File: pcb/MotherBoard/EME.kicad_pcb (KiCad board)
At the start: 2 copper layers, 100 x 60 mm, 48 parts, among them J1 BMP180, J10 Reset, J11 UART2, J12 SPI_CONN, J13 UART0, J14 MQ135, J15 5v, J16 GPIO's, J17 Anemómetro, J19 I2C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

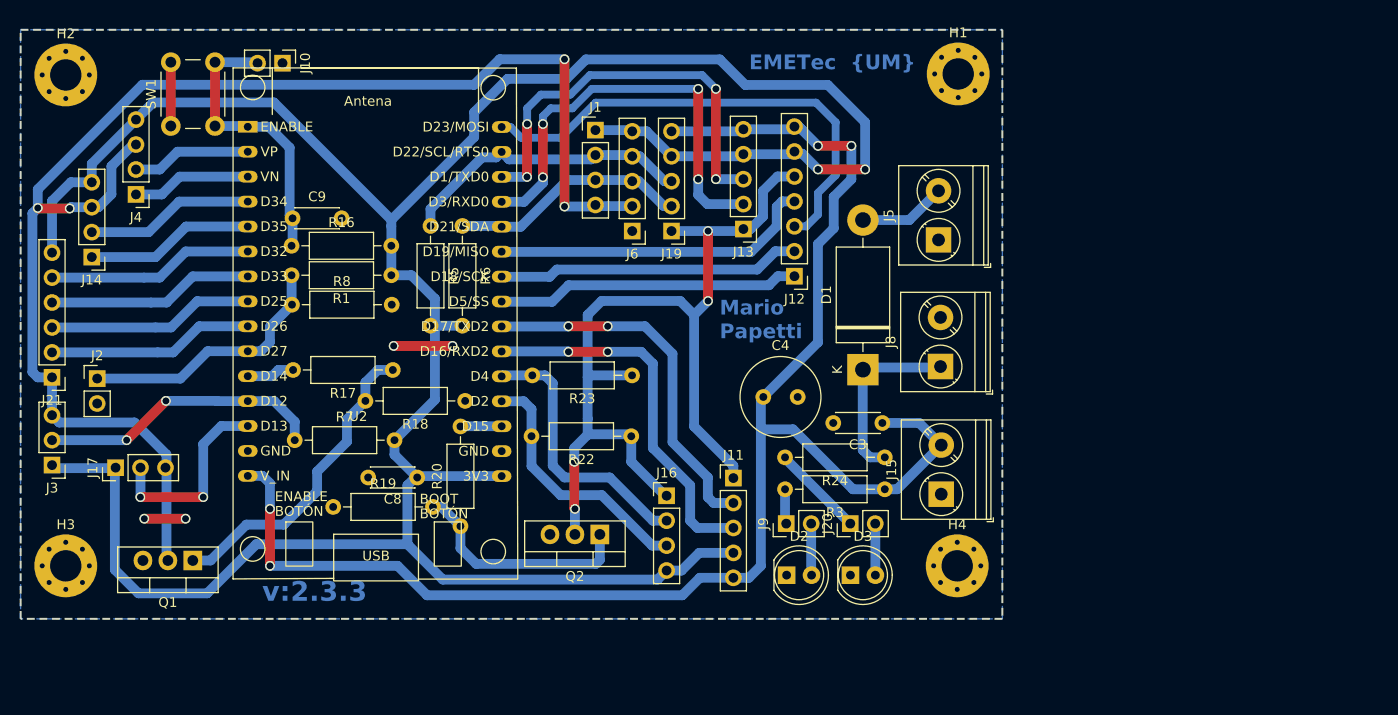
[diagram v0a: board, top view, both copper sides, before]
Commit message: se readaptaron y revisaron las PCBs, listas para imprimir
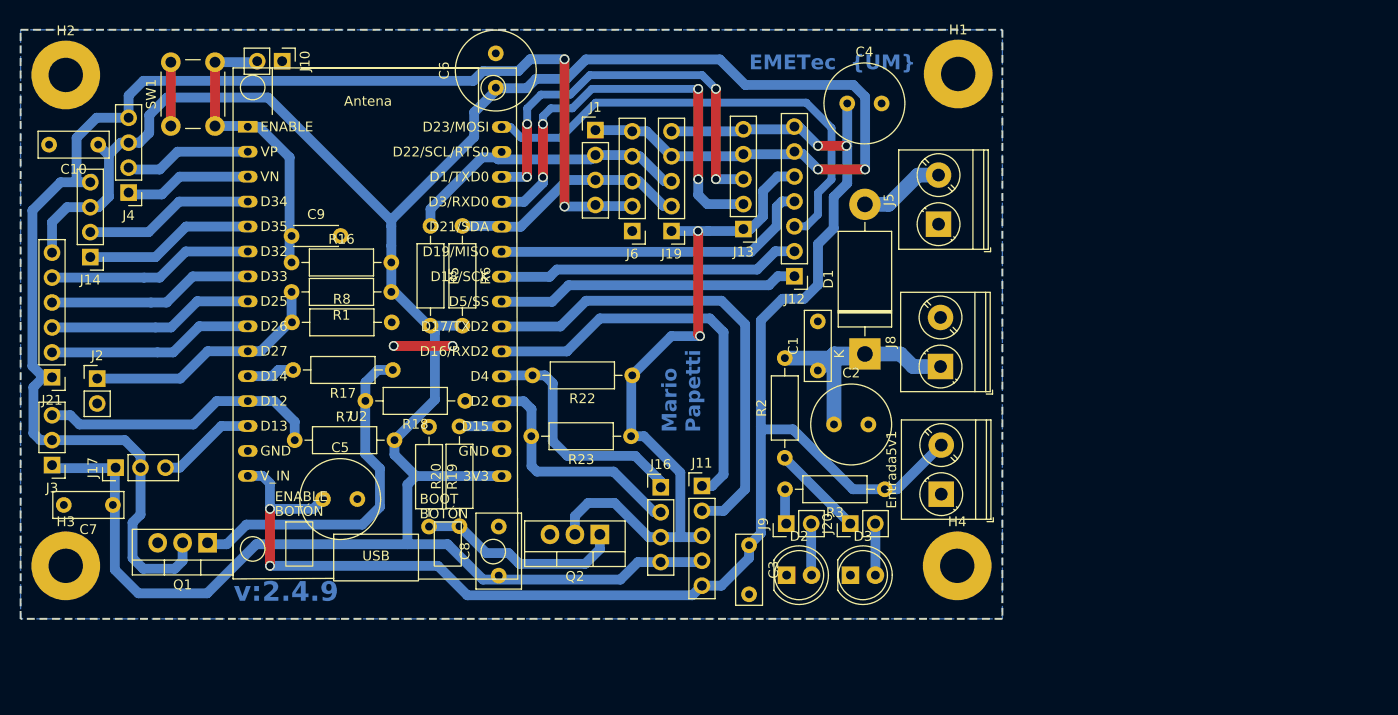
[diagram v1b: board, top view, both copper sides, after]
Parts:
- removed R24: 1k, Resistor_THT:R_Axial_DIN0207_L6.3mm_D2.5mm_P10.16mm_Horizontal
- added C1: 104, Capacitor_THT:C_Disc_D7.0mm_W2.5mm_P5.00mm, F.Cu at (112.4, 89.5)
- added C10: 104, Capacitor_THT:C_Disc_D7.0mm_W2.5mm_P5.00mm, F.Cu at (39.1, 66.5)
- added C2: 220uF, Capacitor_THT:C_Radial_D8.0mm_H11.5mm_P3.50mm, F.Cu at (114.0, 95.0)
- added C5: 22uF, Capacitor_THT:C_Radial_D8.0mm_H7.0mm_P3.50mm, F.Cu at (62.0, 102.6)
- added C6: 22uF, Capacitor_THT:C_Radial_D8.0mm_H7.0mm_P3.50mm, F.Cu at (79.6, 60.7)
- added C7: 104, Capacitor_THT:C_Disc_D7.0mm_W2.5mm_P5.00mm, F.Cu at (40.6, 103.2)
- added R2: 1k, Resistor_THT:R_Axial_DIN0207_L6.3mm_D2.5mm_P10.16mm_Horizontal, F.Cu at (109.0, 98.4)
- C3: footprint Capacitor_THT:C_Disc_D4.3mm_W1.9mm_P5.00mm -> Capacitor_THT:C_Disc_D7.0mm_W2.5mm_P5.00mm
- C8: footprint Capacitor_THT:C_Disc_D4.3mm_W1.9mm_P5.00mm -> Capacitor_THT:C_Disc_D7.5mm_W4.4mm_P5.00mm
- H1, H2, H3, H4: footprint MountingHole:MountingHole_3.2mm_M3_Pad_Via -> MountingHole:MountingHole_3.5mm_Pad
- moved C4 31.1 mm to (115.4, 62.3)
- moved C3 18.4 mm to (105.4, 107.3), turned to -90 degrees
- moved C8 13.0 mm to (79.9, 110.4), turned to 90 degrees
- moved R19 12.7 mm to (72.8, 95.2), turned to -90 degrees
- moved R23 6.20 mm to (93.4, 96.2)
- moved R22 6.20 mm to (93.5, 90.0)
- moved J11 3.30 mm to (100.6, 101.3)
- moved Q1 2.34 mm to (50.2, 107.1)
- moved C9 1.80 mm to (58.8, 75.8)
- moved R8 1.80 mm to (58.8, 84.6)
- moved R1 1.70 mm to (69.0, 81.5)
- moved R16 1.70 mm to (58.8, 78.5)
- moved D1 1.61 mm to (117.2, 87.8)
- moved J5 1.60 mm to (124.7, 74.6)
- moved J16 1.05 mm to (96.4, 101.4)
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- renumbered J15 to Entrada5v1
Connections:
- H1 pad 1: (no net) -> GNDREF
- H2 pad 1: (no net) -> GNDREF
- H3 pad 1: (no net) -> GNDREF
- H4 pad 1: (no net) -> GNDREF
- J11 pad 1: GND_G2 -> RX2
- J11 pad 3: RX2 -> GND_G2
- J14 pad 3: GND_G1 -> +3.3V
- J14 pad 4: +3.3V -> GND_G1
- J16 pad 1: GND_G2 -> GPIO4
- J16 pad 2: GPIO4 -> GPIO13
- J16 pad 3: GPIO13 -> GND_G2
- J17 pad 2: D_hall -> GND_G1
- J17 pad 3: GND_G1 -> D_hall
- J3 pad 2: DHT22 -> GND_G1
- J3 pad 3: GND_G1 -> DHT22
- J4 pad 3: GND_G1 -> +3.3V
- J4 pad 4: +3.3V -> GND_G1
- R22 pad 2: GPIO13 -> GPIO4
- R23 pad 2: GPIO4 -> GPIO13
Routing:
- net GND_G2: track 95.6 -> 71.9 mm, vias 4 -> 2
- net TX2: track 37.5 -> 49.0 mm, vias 2 -> 0
- net +BATT: track 18.6 -> 29.3 mm
- net D_hall: track 20.3 -> 10.3 mm, vias 2 -> 0
- net GNDREF: track 16.7 -> 12.5 mm, vias 4 -> 2
- net Net-(Q1-G): track 32.2 -> 36.1 mm
- net RX2: track 38.2 -> 42.0 mm, vias 2 -> 0
- net GPIO4: track 27.9 -> 24.8 mm
- net +5V: track 159.7 -> 162.4 mm
- net Net-(Q2-G): track 23.5 -> 21.1 mm
- net GPIO13: track 26.3 -> 24.4 mm
- net Div: track 26.9 -> 25.2 mm
- net GND_G1: track 144.6 -> 143.3 mm, vias 4 -> 2
- net Rest: track 29.6 -> 30.6 mm
- net MOSI: track 49.8 -> 48.9 mm
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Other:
- board text added: "v:2.4.9"
- board text removed: "v:2.3.3"

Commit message: Se agregó la modificación del MQ135 a 5v con divisor resistivo; además de cambio del DHT del pin 12; también se modificaron los pines de conexión
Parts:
- removed J16: GPIO's, Connector_PinHeader_2.54mm:PinHeader_1x04_P2.54mm_Vertical
- added C11: 22uF, Capacitor_THT:C_Radial_D8.0mm_H7.0mm_P3.50mm, F.Cu at (143.1, 66.4)
- added C12: 104, Capacitor_THT:C_Disc_D7.0mm_W2.5mm_P5.00mm, F.Cu at (106.2, 114.9)
- added J7: MQ135, Connector_PinHeader_2.54mm:PinHeader_1x03_P2.54mm_Vertical, F.Cu at (80.9, 104.8)
- added R10: 22k, Resistor_THT:R_Axial_DIN0207_L6.3mm_D2.5mm_P10.16mm_Horizontal, F.Cu at (76.8, 98.4)
- added R9: 12k, Resistor_THT:R_Axial_DIN0207_L6.3mm_D2.5mm_P10.16mm_Horizontal, F.Cu at (76.8, 101.4)
- J14: value MQ135 -> GPIO's; footprint Connector_PinHeader_2.54mm:PinHeader_1x04_P2.54mm_Vertical -> Connector_PinHeader_2.54mm:PinHeader_1x05_P2.54mm_Vertical
- R1: value 4k7 -> 1M
- R8: value 4k7 -> 180k
- moved J14 104.5 mm to (134.8, 118.0)
- moved C8 46.0 mm to (102.0, 70.1)
- moved J2 43.4 mm to (82.3, 92.3)
- moved J3 40.3 mm to (70.5, 81.2), turned to 90 degrees
- moved J17 40.0 mm to (79.0, 111.2)
- moved R7 39.6 mm to (95.2, 80.2)
- moved J21 39.5 mm to (73.2, 97.7)
- moved J4 39.1 mm to (80.8, 77.8)
- moved D2 38.9 mm to (147.4, 118.1)
- moved D3 38.9 mm to (153.9, 118.1)
- moved Entrada_5v1 38.9 mm to (163.1, 109.8)
- moved H4 38.9 mm to (164.8, 117.1)
- moved J11 38.9 mm to (138.8, 109.0)
- moved J13 38.9 mm to (143.0, 82.8)
- moved R23 38.9 mm to (131.6, 103.9)
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- renumbered Entrada5v1 to Entrada_5v1
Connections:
- J14 pad 1: MQ135_An -> +3.3V
- J14 pad 2: MQ135_Dg -> GND_G2
- J14 pad 3: +3.3V -> GPIO12
- J14 pad 4: GND_G1 -> GPIO2
- J3 pad 1: +3.3V -> GND_G1
- J3 pad 2: GND_G1 -> +3.3V
- R23 pad 2: GPIO13 -> GPIO2
- U2 pad 10: Div -> MQ135_An
- U2 pad 12: DHT22 -> GPIO12
- U2 pad 19: GPIO13 -> GPIO2
- U2 pad 4: MQ135_Dg -> DHT22
- U2 pad 5: MQ135_An -> S0
- U2 pad 6: S0 -> S1
- U2 pad 7: S1 -> S2
- U2 pad 8: S2 -> Y
- U2 pad 9: Y -> Div
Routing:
- net GPIO12: track 0.00 -> 52.9 mm, vias 0 -> 2
- net GPIO13: track 24.4 -> 0.00 mm
- net GPIO2: track 0.00 -> 23.4 mm
- net +5V: track 162.4 -> 180.0 mm, vias 4 -> 6
- net MQ135_Dg: track 17.2 -> 0.00 mm
- net DHT22: track 28.8 -> 20.1 mm
- net Div: track 25.2 -> 18.0 mm
- net GND_G2: track 71.9 -> 76.7 mm
- net Net-(J7-Pin_3): track 0.00 -> 3.81 mm
- net D_hall: track 10.3 -> 13.6 mm
- net GND_G1: track 143.3 -> 141.2 mm
- net Net-(Q1-G): track 36.1 -> 34.2 mm
- net Rest: track 30.6 -> 32.2 mm
- net MQ135_An: track 17.2 -> 18.2 mm
- net RX2: track 42.0 -> 41.3 mm
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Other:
- board text added: "EMETec"
- board text added: "v:2.5.5"
- board text removed: "EMETec {UM}"
- board text removed: "v:2.4.9"
